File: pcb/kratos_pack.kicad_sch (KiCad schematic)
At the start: 97 parts, among them J1 USB_C_Receptacle_USB2.0, J2 PROG_CONN, J3 DBG_UART, J4 BAT_MID+NTC, J5 BAT_7.4V, J6 BAT_0V, J7 OUT+, J8 OUT-, Q1 AON7403, Q2 AON7414, Q3 AON7414, SW1 WAKEUP, SW2 BOOT, SW3 RST_BTN, U1 USBLC6-2SC6, U10 24LC32, U2 CP2102N-Axx-xQFN20, U3 STM32G071Gx, U4 KTD2026BEWE, U5 BQ25887, U6 BD48xxFVE, U7 INA199, U8 LTC4231, U9 LDK715M33R

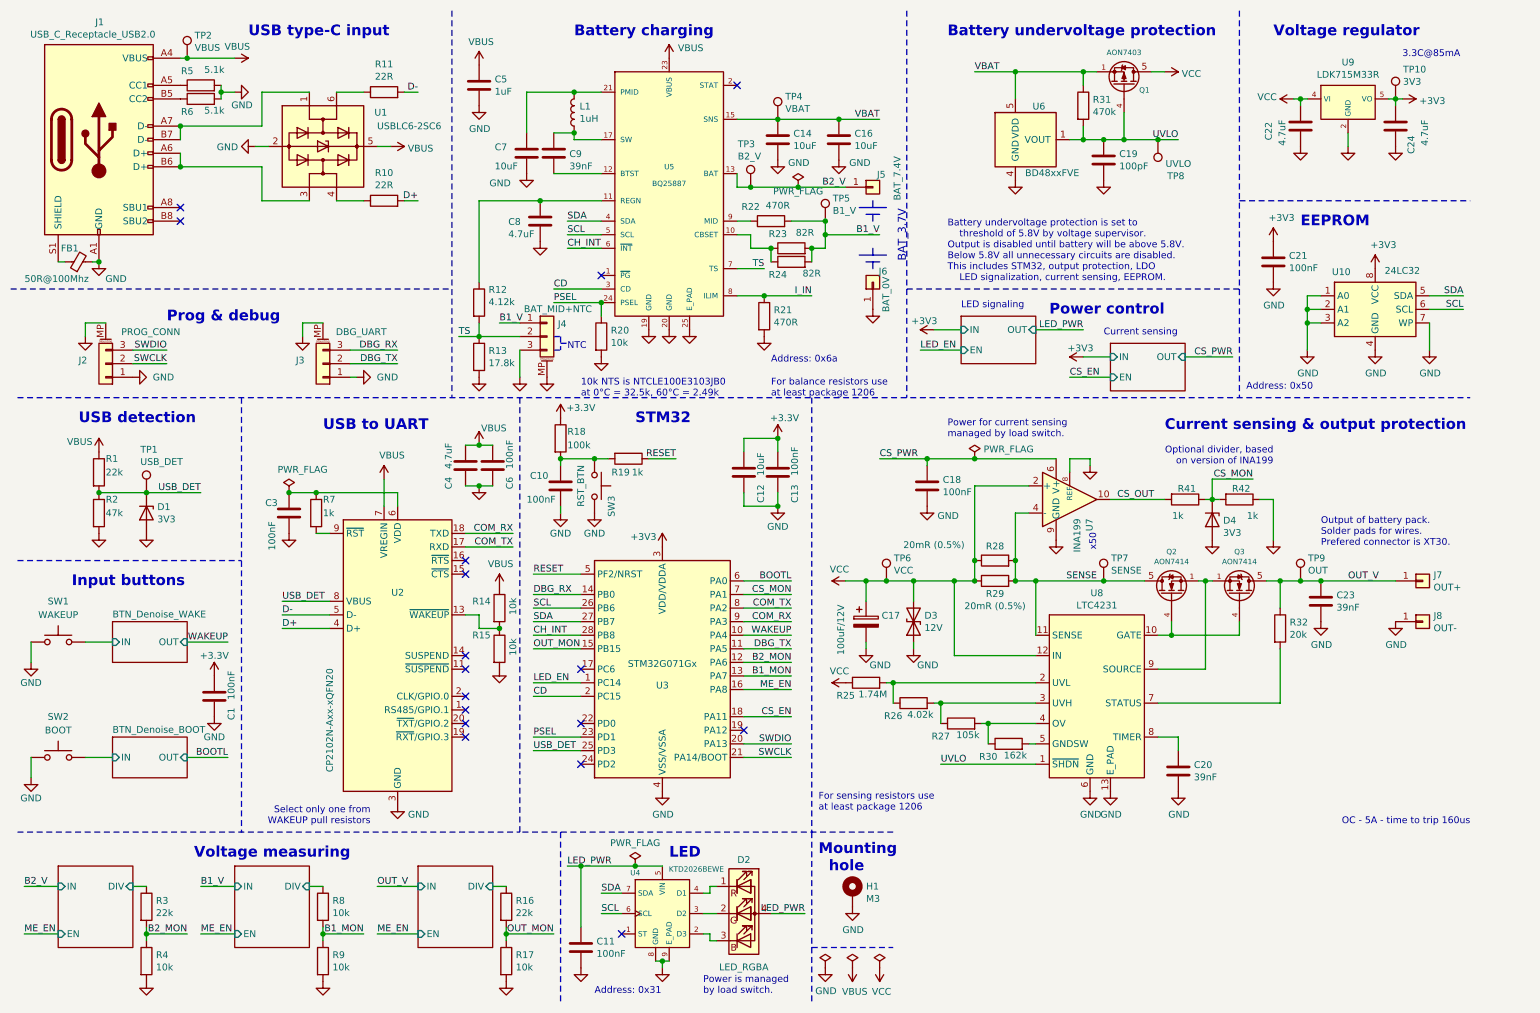
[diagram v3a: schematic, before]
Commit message: Schema & PCB: reconect output of charger from SNS to VBAT
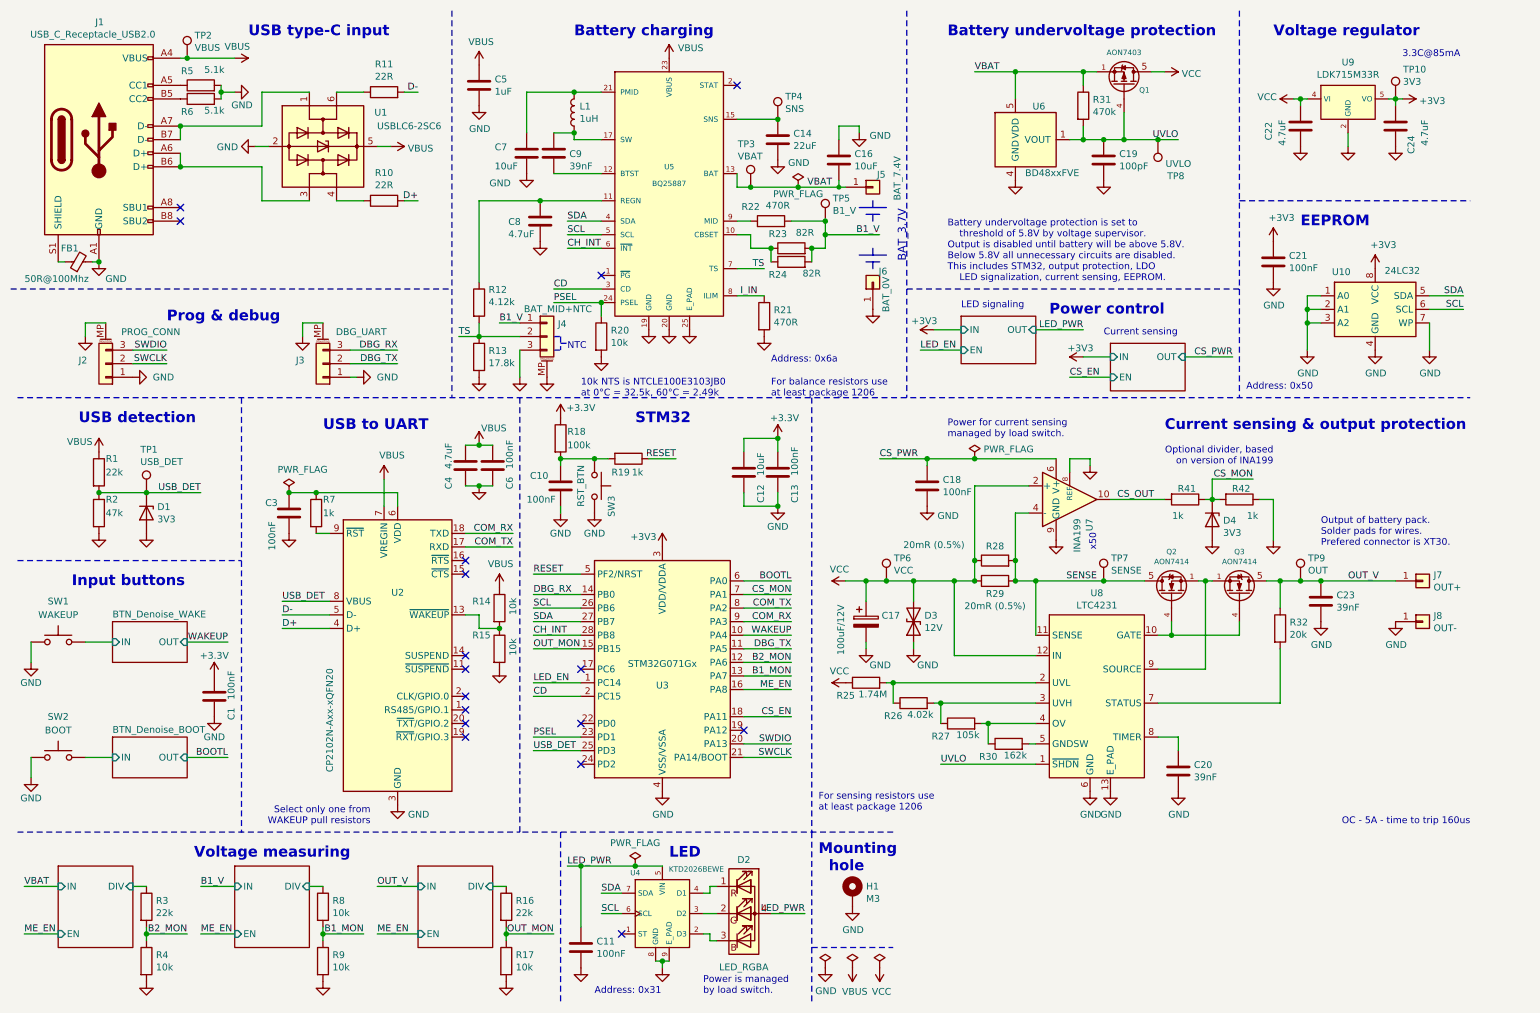
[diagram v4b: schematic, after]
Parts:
- C14: value 10uF -> 22uF
- TP3: value B2_V -> VBAT
- TP4: value VBAT -> SNS
- U7: symbol TCY_IC:INA199 -> TCY_power_management:INA199
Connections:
- net B2_V is gone; now on net VBAT: J5.1 (Pin_1), TP3.1, U5.13 (BAT), U5.14 (BAT)
- net GND: now also C16.1; no longer C16.2
- net VBAT: now also C16.2; no longer C14.1, C16.1, TP4.1, U5.15 (SNS), U5.16 (SNS)
- new net: C14.1, TP4.1, U5.15 (SNS), U5.16 (SNS)
- new net: U7.1 (NC), U7.7 (NC)
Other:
- moved on the sheet: C16
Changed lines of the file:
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@@
   (title_block
     (title "Kratos pack")
-    (date "2020-12-18")
-    (rev "v1.0")
+    (date "2022-07-01")
+    (rev "v1.1")
     (company "Author: Petr Malaník")
   )
@@
   (junction (at 180.34 119.38) (diameter 1.016) (color 0 0 0 0)
   )
-  (junction (at 152.4 66.04) (diameter 1.016) (color 0 0 0 0)
-  )
   (junction (at 191.77 115.57) (diameter 1.016) (color 0 0 0 0)
   )
@@
   (junction (at 163.83 54.61) (diameter 1.016) (color 0 0 0 0)
   )
-  (junction (at 166.37 33.02) (diameter 1.016) (color 0 0 0 0)
-  )
   (junction (at 228.6 129.54) (diameter 1.016) (color 0 0 0 0)
   )
@@
   (junction (at 175.26 119.38) (diameter 1.016) (color 0 0 0 0)
   )
+  (junction (at 166.37 45.72) (diameter 0) (color 0 0 0 0)
+  )
   (junction (at 27.94 102.87) (diameter 1.016) (color 0 0 0 0)
   )
@@
     (stroke (width 0) (type solid) (color 0 0 0 0))
   )
+  (wire (pts (xy 166.37 34.29) (xy 166.37 36.83))
+    (stroke (width 0) (type default) (color 0 0 0 0))
+  )
   (wire (pts (xy 133.35 190.5) (xy 133.35 191.77))
     (stroke (width 0) (type solid) (color 0 0 0 0))
@@
     (stroke (width 0) (type solid) (color 0 0 0 0))
   )
-  (wire (pts (xy 154.94 33.02) (xy 166.37 33.02))
-    (stroke (width 0) (type solid) (color 0 0 0 0))
-  )
   (wire (pts (xy 153.67 181.61) (xy 160.02 181.61))
     (stroke (width 0) (type solid) (color 0 0 0 0))
@@
     (stroke (width 0) (type solid) (color 0 0 0 0))
   )
+  (wire (pts (xy 170.18 35.56) (xy 170.18 34.29))
+    (stroke (width 0) (type default) (color 0 0 0 0))
+  )
   (wire (pts (xy 66.04 71.12) (xy 69.85 71.12))
     (stroke (width 0) (type solid) (color 0 0 0 0))
@@
     (stroke (width 0) (type dash) (color 0 0 0 0))
   )
+  (wire (pts (xy 166.37 45.72) (xy 167.64 45.72))
+    (stroke (width 0) (type solid) (color 0 0 0 0))
+  )
   (wire (pts (xy 236.22 104.14) (xy 237.49 104.14))
     (stroke (width 0) (type solid) (color 0 0 0 0))
@@
     (stroke (width 0) (type solid) (color 0 0 0 0))
   )
-  (wire (pts (xy 166.37 33.02) (xy 173.99 33.02))
-    (stroke (width 0) (type solid) (color 0 0 0 0))
-  )
   (wire (pts (xy 270.51 29.21) (xy 271.78 29.21))
     (stroke (width 0) (type solid) (color 0 0 0 0))
@@
     (stroke (width 0) (type solid) (color 0 0 0 0))
   )
+  (wire (pts (xy 170.18 34.29) (xy 166.37 34.29))
+    (stroke (width 0) (type default) (color 0 0 0 0))
+  )
   (polyline (pts (xy 161.29 187.96) (xy 176.53 187.96))
     (stroke (width 0) (type dash) (color 0 0 0 0))
@@
     (stroke (width 0) (type solid) (color 0 0 0 0))
   )
+  (wire (pts (xy 158.75 45.72) (xy 166.37 45.72))
+    (stroke (width 0) (type solid) (color 0 0 0 0))
+  )
   (wire (pts (xy 107.95 35.56) (xy 107.95 27.94))
     (stroke (width 0) (type solid) (color 0 0 0 0))
@@
     (stroke (width 0) (type solid) (color 0 0 0 0))
   )
-  (wire (pts (xy 152.4 66.04) (xy 161.29 66.04))
-    (stroke (width 0) (type solid) (color 0 0 0 0))
-  )
   (wire (pts (xy 276.86 66.04) (xy 283.21 66.04))
     (stroke (width 0) (type solid) (color 0 0 0 0))
@@
     (stroke (width 0) (type solid) (color 0 0 0 0))
   )
+  (wire (pts (xy 166.37 44.45) (xy 166.37 45.72))
+    (stroke (width 0) (type default) (color 0 0 0 0))
+  )
   (wire (pts (xy 148.59 149.86) (xy 157.48 149.86))
     (stroke (width 0) (type solid) (color 0 0 0 0))
@@
     (stroke (width 0) (type dash) (color 0 0 0 0))
   )
-  (wire (pts (xy 158.75 45.72) (xy 167.64 45.72))
-    (stroke (width 0) (type solid) (color 0 0 0 0))
-  )
   (wire (pts (xy 173.99 96.52) (xy 182.88 96.52))
     (stroke (width 0) (type solid) (color 0 0 0 0))
@@
     (effects (font (size 1.27 1.27)) (justify right bottom))
   )
-  (label "B2_V" (at 13.97 176.53 0)
+  (label "VBAT" (at 13.97 176.53 0)
     (effects (font (size 1.27 1.27)) (justify left bottom))
   )
@@
     (effects (font (size 1.27 1.27)) (justify right bottom))
   )
-  (label "VBAT" (at 173.99 33.02 180)
+  (label "VBAT" (at 165.1 45.72 180)
     (effects (font (size 1.27 1.27)) (justify right bottom))
   )
@@
     (effects (font (size 1.27 1.27)) (justify left bottom))
   )
-  (label "I_IN" (at 161.29 66.04 180)
-    (effects (font (size 1.27 1.27)) (justify right bottom))
-  )
-  (label "B2_V" (at 167.64 45.72 180)
+  (label "I_IN" (at 151.13 66.04 180)
     (effects (font (size 1.27 1.27)) (justify right bottom))
   )
@@
       (effects (font (size 1.27 1.27)) (justify left))
     )
-    (property "Value" "B2_V" (id 1) (at 147.447 39.948 0)
+    (property "Value" "VBAT" (id 1) (at 147.447 39.948 0)
       (effects (font (size 1.27 1.27)) (justify left))
     )
@@
       (effects (font (size 1.27 1.27)) hide)
     )
+    (pin "1")
     (pin "2")
+    (pin "3")
     (pin "4")
     (pin "5")
@@
     (pin "1")
   )
-  (symbol (lib_id "Device:C") (at 166.37 36.83 0) (unit 1)
+  (symbol (lib_id "Device:C") (at 166.37 40.64 0) (unit 1)
     (in_bom yes) (on_board yes)
-    (property "Reference" "C16" (id 0) (at 169.2911 35.6806 0)
+    (property "Reference" "C16" (id 0) (at 169.2911 39.4906 0)
       (effects (font (size 1.27 1.27)) (justify left))
     )
-    (property "Value" "10uF" (id 1) (at 169.291 37.979 0)
+    (property "Value" "10uF" (id 1) (at 169.291 41.789 0)
       (effects (font (size 1.27 1.27)) (justify left))
     )
-    (property "Footprint" "Capacitor_SMD:C_0805_2012Metric" (id 2) (at 167.3352 40.64 0)
+    (property "Footprint" "Capacitor_SMD:C_0805_2012Metric" (id 2) (at 167.3352 44.45 0)
       (effects (font (size 1.27 1.27)) hide)
     )
-    (property "Datasheet" "~" (id 3) (at 166.37 36.83 0)
+    (property "Datasheet" "~" (id 3) (at 166.37 40.64 0)
       (effects (font (size 1.27 1.27)) hide)
     )
@@
       (effects (font (size 1.27 1.27)) hide)
     )
-    (property "Value" "PWR_FLAG" (id 1) (at 158.75 46.4756 0))
+    (property "Value" "PWR_FLAG" (id 1) (at 158.75 46.99 0))
     (property "Footprint" "" (id 2) (at 158.75 45.72 0)
       (effects (font (size 1.27 1.27)) hide)
@@
     (pin "1")
     (pin "2")
+    (pin "3")
     (pin "4")
     (pin "5")
@@
     (pin "2")
   )
-  (symbol (lib_id "TCY_IC:INA199") (at 209.55 104.14 0) (unit 1)
+  (symbol (lib_id "TCY_power_management:INA199") (at 209.55 104.14 0) (unit 1)
     (in_bom yes) (on_board yes)
     (property "Reference" "U7" (id 0) (at 213.2394 107.6961 90)
@@
       (effects (font (size 1.27 1.27)) (justify right))
     )
-    (property "Footprint" "Package_DFN_QFN:UQFN-10_1.4x1.8mm_P0.4mm" (id 2) (at 209.55 104.14 0)
+    (property "Footprint" "Package_DFN_QFN:UQFN-10_1.4x1.8mm_P0.4mm" (id 2) (at 209.55 125.73 0)
       (effects (font (size 1.27 1.27)) hide)
     )
-    (property "Datasheet" "https://www.ti.com/lit/ds/symlink/ina199.pdf" (id 3) (at 209.55 104.14 0)
+    (property "Datasheet" "https://www.ti.com/lit/ds/symlink/ina199.pdf" (id 3) (at 209.55 123.19 0)
       (effects (font (size 1.27 1.27)) hide)
     )
+    (pin "1")
     (pin "10")
     (pin "2")
@@
     (pin "5")
     (pin "6")
+    (pin "7")
     (pin "8")
     (pin "9")
@@
       (effects (font (size 1.27 1.27)) (justify left))
     )
-    (property "Value" "10uF" (id 1) (at 157.861 37.979 0)
+    (property "Value" "22uF" (id 1) (at 157.861 37.979 0)
       (effects (font (size 1.27 1.27)) (justify left))
     )
@@
     (pin "2")
   )
-  (symbol (lib_id "power:GND") (at 166.37 40.64 0) (unit 1)
+  (symbol (lib_id "power:GND") (at 170.18 35.56 0) (unit 1)
     (in_bom yes) (on_board yes)
-    (property "Reference" "#PWR048" (id 0) (at 166.37 46.99 0)
+    (property "Reference" "#PWR048" (id 0) (at 170.18 41.91 0)
       (effects (font (size 1.27 1.27)) hide)
     )
-    (property "Value" "GND" (id 1) (at 170.2943 41.1544 0))
-    (property "Footprint" "" (id 2) (at 166.37 40.64 0)
+    (property "Value" "GND" (id 1) (at 174.1043 36.0744 0))
+    (property "Footprint" "" (id 2) (at 170.18 35.56 0)
       (effects (font (size 1.27 1.27)) hide)
     )
-    (property "Datasheet" "" (id 3) (at 166.37 40.64 0)
+    (property "Datasheet" "" (id 3) (at 170.18 35.56 0)
       (effects (font (size 1.27 1.27)) hide)
     )
@@
       (effects (font (size 1.27 1.27)) (justify left))
     )
-    (property "Value" "VBAT" (id 1) (at 156.337 31.058 0)
+    (property "Value" "SNS" (id 1) (at 156.337 31.058 0)
       (effects (font (size 1.27 1.27)) (justify left))
     )
@@
     )
     (path "/b50a2cfa-ab81-49ca-bda0-304e9e4e5207"
-      (reference "C14") (unit 1) (value "10uF") (footprint "Capacitor_SMD:C_0805_2012Metric")
+      (reference "C14") (unit 1) (value "22uF") (footprint "Capacitor_SMD:C_0805_2012Metric")
     )
     (path "/0cd4cbb4-c953-49af-8dbf-3827f43e5681"
@@
     )
     (path "/0147a5a6-2f1a-4a67-824a-50b41cec44a8"
-      (reference "TP3") (unit 1) (value "B2_V") (footprint "TCY_connectors:TestPoint_Pad_D0.5mm")
+      (reference "TP3") (unit 1) (value "VBAT") (footprint "TCY_connectors:TestPoint_Pad_D0.5mm")
     )
     (path "/ea3c2e2e-3973-4fda-8182-d29f1ee77c88"
-      (reference "TP4") (unit 1) (value "VBAT") (footprint "TCY_connectors:TestPoint_Pad_D0.5mm")
+      (reference "TP4") (unit 1) (value "SNS") (footprint "TCY_connectors:TestPoint_Pad_D0.5mm")
     )
     (path "/dbf1e4a4-28db-44a7-aa3b-665ecbe5f131"

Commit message: PCB: change footprint of resistors and capacitors to smaller version
After first version is apparent that smaller footprint used on some
resistors are big enough for manual soldering. Because of this was
exchanged for custom smaller version.

In current version pull-up resistor of reset circuit is not connected,
because is mend to be removed in future.
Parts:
- C1, C10, C11, C13, C18, C19, C20, C21, C22, C23, C24, C3, C4, C5, C6, C8, C9: footprint Capacitor_SMD:C_0603_1608Metric -> TCY_passives:C_0603_1608Metric
- C12, C14, C16, C7: footprint Capacitor_SMD:C_0805_2012Metric -> TCY_passives:C_0805_2012Metric
- R1, R10, R11, R12, R13, R14, R15, R16, R17, R18, R19, R2, R20, R21, R22, R25, R26, R27, R3, R30, R31, R32, R4, R41, R42, R5, R6, R7, R8, R9: footprint Resistor_SMD:R_0603_1608Metric -> TCY_passives:R_0603_1608Metric

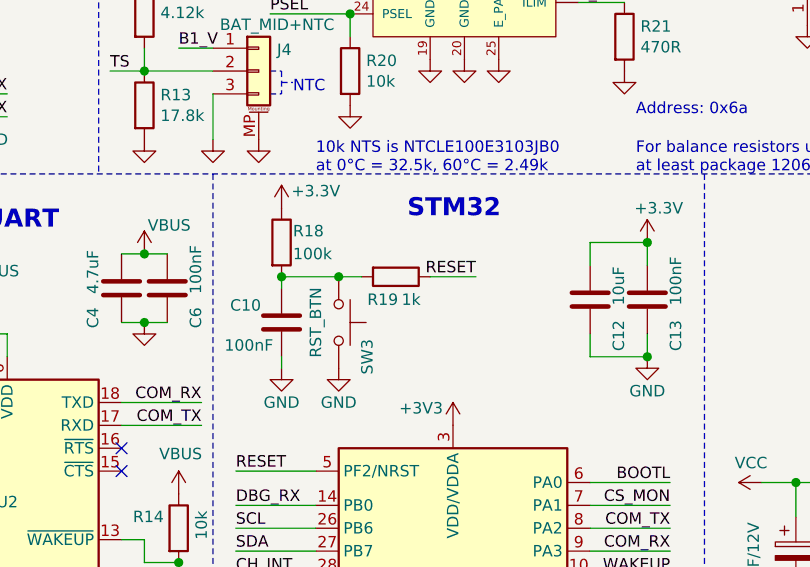
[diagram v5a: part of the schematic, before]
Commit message: Schema & PCB: Remove resistor in series with RESET line
Also some passive components around was shifter which resulted in better
clearance from edge of PCB.
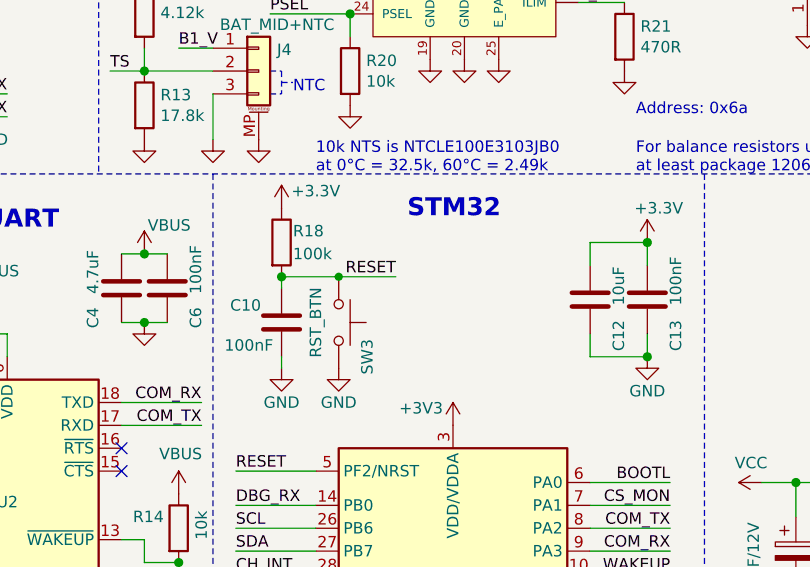
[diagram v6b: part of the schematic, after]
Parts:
- removed R19: 1k, TCY_passives:R_0603_1608Metric, symbol Device:R
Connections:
- net RESET: now also C10.1, R18.2, SW3.1
- net at U7.1 (NC): no longer U7.7 (NC)
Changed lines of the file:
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@@
   (junction (at 99.06 101.6) (diameter 1.016) (color 0 0 0 0)
   )
-  (junction (at 120.65 96.52) (diameter 1.016) (color 0 0 0 0)
-  )
   (junction (at 248.92 119.38) (diameter 1.016) (color 0 0 0 0)
   )
@@
   (junction (at 182.88 96.52) (diameter 1.016) (color 0 0 0 0)
   )
+  (junction (at 120.65 96.52) (diameter 0) (color 0 0 0 0)
+  )
   (junction (at 154.94 105.41) (diameter 1.016) (color 0 0 0 0)
   )
@@
     (stroke (width 0) (type solid) (color 0 0 0 0))
   )
-  (wire (pts (xy 120.65 96.52) (xy 123.19 96.52))
-    (stroke (width 0) (type solid) (color 0 0 0 0))
-  )
   (wire (pts (xy 34.29 76.2) (xy 40.64 76.2))
     (stroke (width 0) (type solid) (color 0 0 0 0))
@@
     (stroke (width 0) (type solid) (color 0 0 0 0))
   )
-  (wire (pts (xy 130.81 96.52) (xy 135.89 96.52))
-    (stroke (width 0) (type solid) (color 0 0 0 0))
-  )
   (wire (pts (xy 116.84 35.56) (xy 116.84 36.83))
     (stroke (width 0) (type solid) (color 0 0 0 0))
@@
     (stroke (width 0) (type solid) (color 0 0 0 0))
   )
+  (wire (pts (xy 120.65 96.52) (xy 127 96.52))
+    (stroke (width 0) (type default) (color 0 0 0 0))
+  )
   (wire (pts (xy 99.06 73.66) (xy 106.68 73.66))
     (stroke (width 0) (type solid) (color 0 0 0 0))
@@
     (effects (font (size 1.27 1.27)) (justify right bottom))
   )
-  (label "RESET" (at 135.89 96.52 180)
+  (label "RESET" (at 127 96.52 180)
     (effects (font (size 1.27 1.27)) (justify right bottom))
   )
@@
     (pin "1")
   )
-  (symbol (lib_id "Device:R") (at 127 96.52 270) (unit 1)
-    (in_bom yes) (on_board yes)
-    (property "Reference" "R19" (id 0) (at 123.825 99.06 90)
-      (effects (font (size 1.27 1.27)) (justify left))
-    )
-    (property "Value" "1k" (id 1) (at 127.635 99.06 90)
-      (effects (font (size 1.27 1.27)) (justify left))
-    )
-    (property "Footprint" "TCY_passives:R_0603_1608Metric" (id 2) (at 127 94.742 90)
-      (effects (font (size 1.27 1.27)) hide)
-    )
-    (property "Datasheet" "~" (id 3) (at 127 96.52 0)
-      (effects (font (size 1.27 1.27)) hide)
-    )
-    (pin "1")
-    (pin "2")
-  )
   (symbol (lib_id "power:GND") (at 133.35 191.77 0) (unit 1)
     (in_bom yes) (on_board yes)
@@
       (reference "R18") (unit 1) (value "100k") (footprint "TCY_passives:R_0603_1608Metric")
     )
-    (path "/aa9a8b43-d229-4369-a302-d9c121359f40"
-      (reference "R19") (unit 1) (value "1k") (footprint "TCY_passives:R_0603_1608Metric")
-    )
     (path "/711a1579-d6f0-4088-a2f0-c528bdbc76ff"
